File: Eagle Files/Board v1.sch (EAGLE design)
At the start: 9 parts

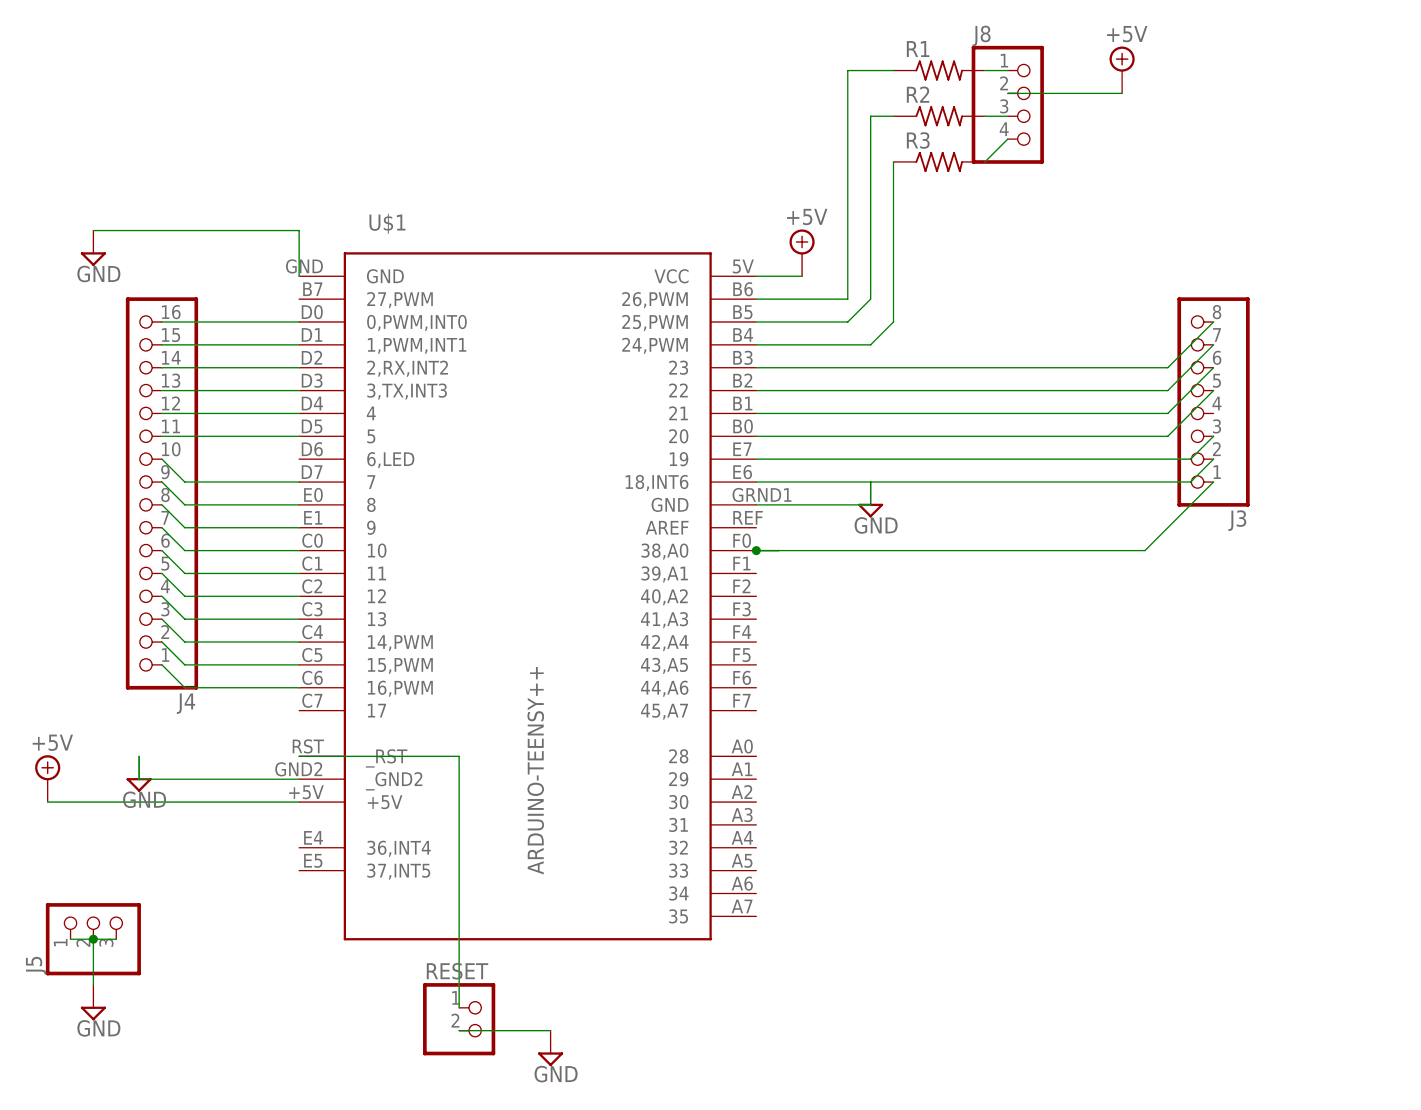
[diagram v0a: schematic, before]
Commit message: Modified schematic and board for 16/12 and 16/8/4 pin connector setups.
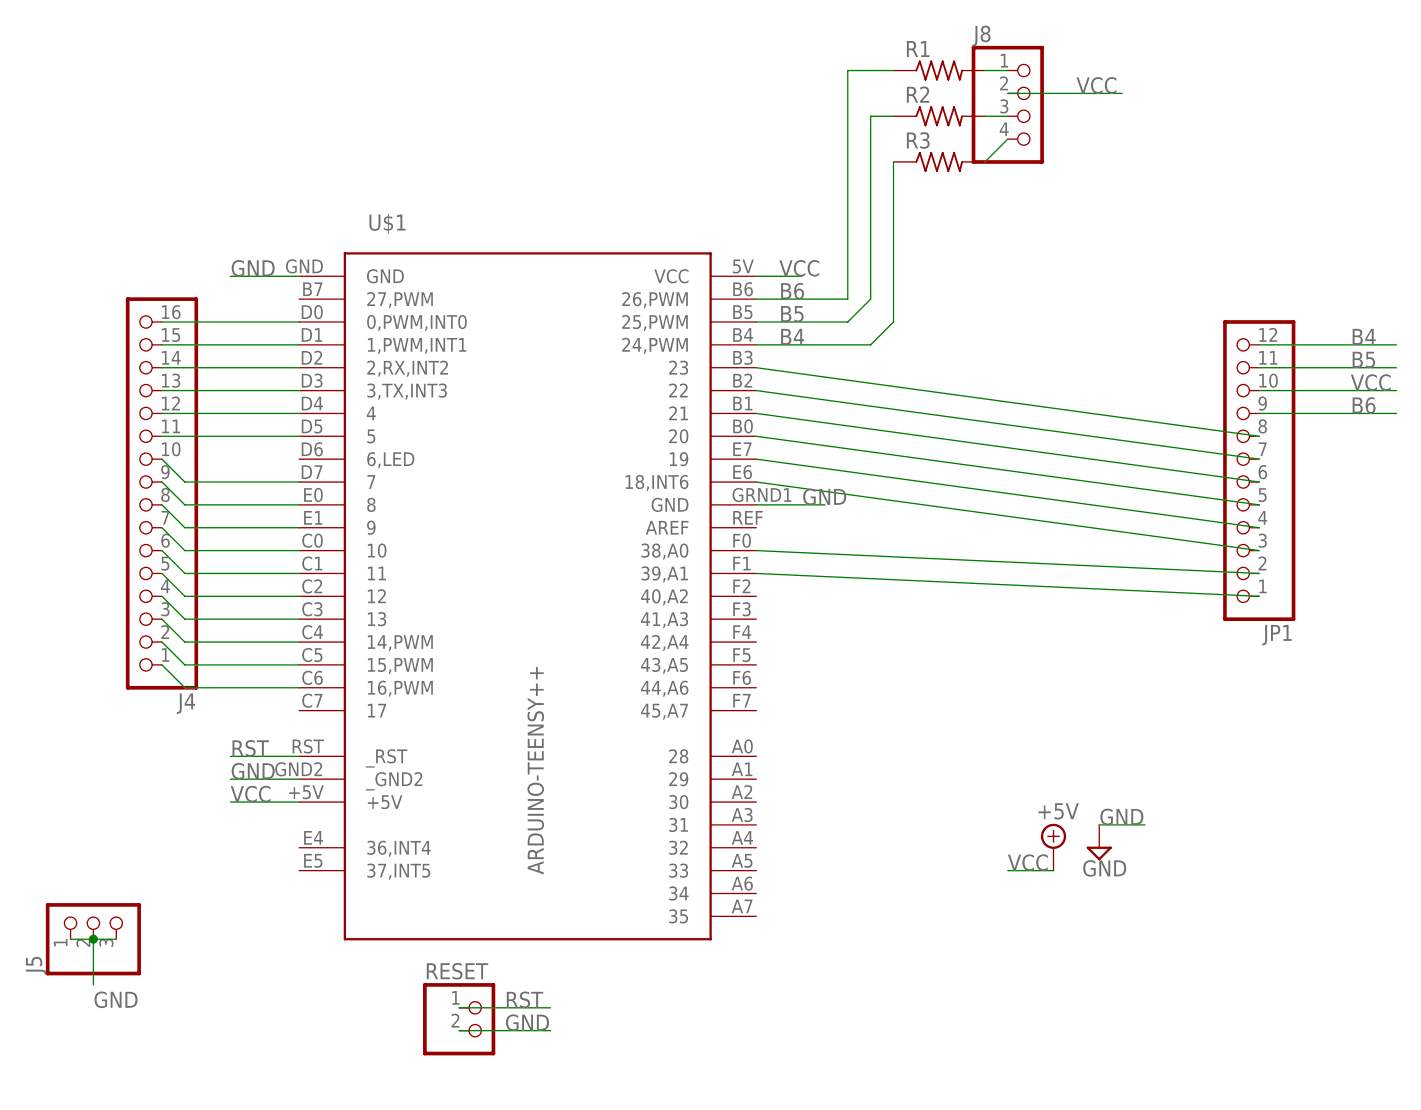
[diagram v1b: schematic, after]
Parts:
- removed J3: (no value), pinhead:PINHD-1X8
- added JP1: (no value), pinhead:PINHD-1X12
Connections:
- net N$31 renamed RST
- removed net +5V: J8.2, U$1.+5V, U$1.VCC
- removed net N$20: R1.1, U$1.26,PWM
- removed net N$21: R2.1, U$1.25,PWM
- removed net N$22: R3.1, U$1.24,PWM
- new net B4: JP1.12, R3.1, U$1.24,PWM
- new net B5: JP1.11, R2.1, U$1.25,PWM
- new net B6: JP1.9, R1.1, U$1.26,PWM
- new net N$30: JP1.1, U$1.39,A1
- new net VCC: J8.2, JP1.10, U$1.+5V, U$1.VCC
- net N$23: now also JP1.8; no longer J3.8
- net N$24: now also JP1.7; no longer J3.7
- net N$25: now also JP1.6; no longer J3.6
- net N$26: now also JP1.5; no longer J3.5
- net N$27: now also JP1.4; no longer J3.3
- net N$28: now also JP1.3, U$1.18,INT6; no longer J3.1, U$1.38,A0
- net N$29: now also JP1.2, U$1.38,A0; no longer J3.2, U$1.18,INT6
